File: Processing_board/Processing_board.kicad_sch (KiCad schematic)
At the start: 21 parts, among them J1 Conn_01x06_Pin, J10 Conn_01x03_Pin, J4 Conn_01x02_Pin, J5 Conn_01x08_Pin, J6 Conn_01x08_Pin, J7 Conn_01x02_Pin, J9 Conn_01x03_Pin, SW1 SW_Push, SW2 SW_Push, U1 STM32WBA63CIU6

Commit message: 3 RF antennas
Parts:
- removed D8: IN_S42BT LED, symbol Device:LED
- added D9: IN_S42BT LED, symbol Device:LED
- added R14, R15, R16, R17, R18: 100R, symbol Device:R_Small
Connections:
- net 3.3V: no longer J1.2 (Pin_2), SW2.1
- net GND: now also J1.2 (Pin_2), R18.1; no longer J1.1 (Pin_1)
- net LED: now also D9.2 (A)
- net USART2_RX: now also R15.1; no longer U1.23 (PB4)
- net USART2_TX: now also R14.1; no longer U1.32 (PB0)
- net ANT_LOGIC_2: now reaches U1.10 (PA2)
- net ANT_LOGIC_1: now reaches U1.12 (PA1)
- net RF: now reaches U1.37 (RF)
- net at U1.6 (PA7): now also R17.2; no longer J9.3 (Pin_3)
- net at U1.9 (PA5): now also R16.2; no longer J9.2 (Pin_2)
- new net: R15.2, U1.23 (PB4)
- new net: R14.2, U1.32 (PB0)
- new net: D9.1 (K), R18.2
- new net +3.3V: J1.1 (Pin_1), SW2.1
- new net USART3_RX: J9.3 (Pin_3), R17.1
- new net USART3_TX: J9.2 (Pin_2), R16.1
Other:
- added sheet RF circuitry & antennas (RF.kicad_sch)
- note added: "GND"
- note added: "The 100R resistor is ESD protection apparently"
- note added: "VCC"
- moved on the sheet: J1, J10, J9

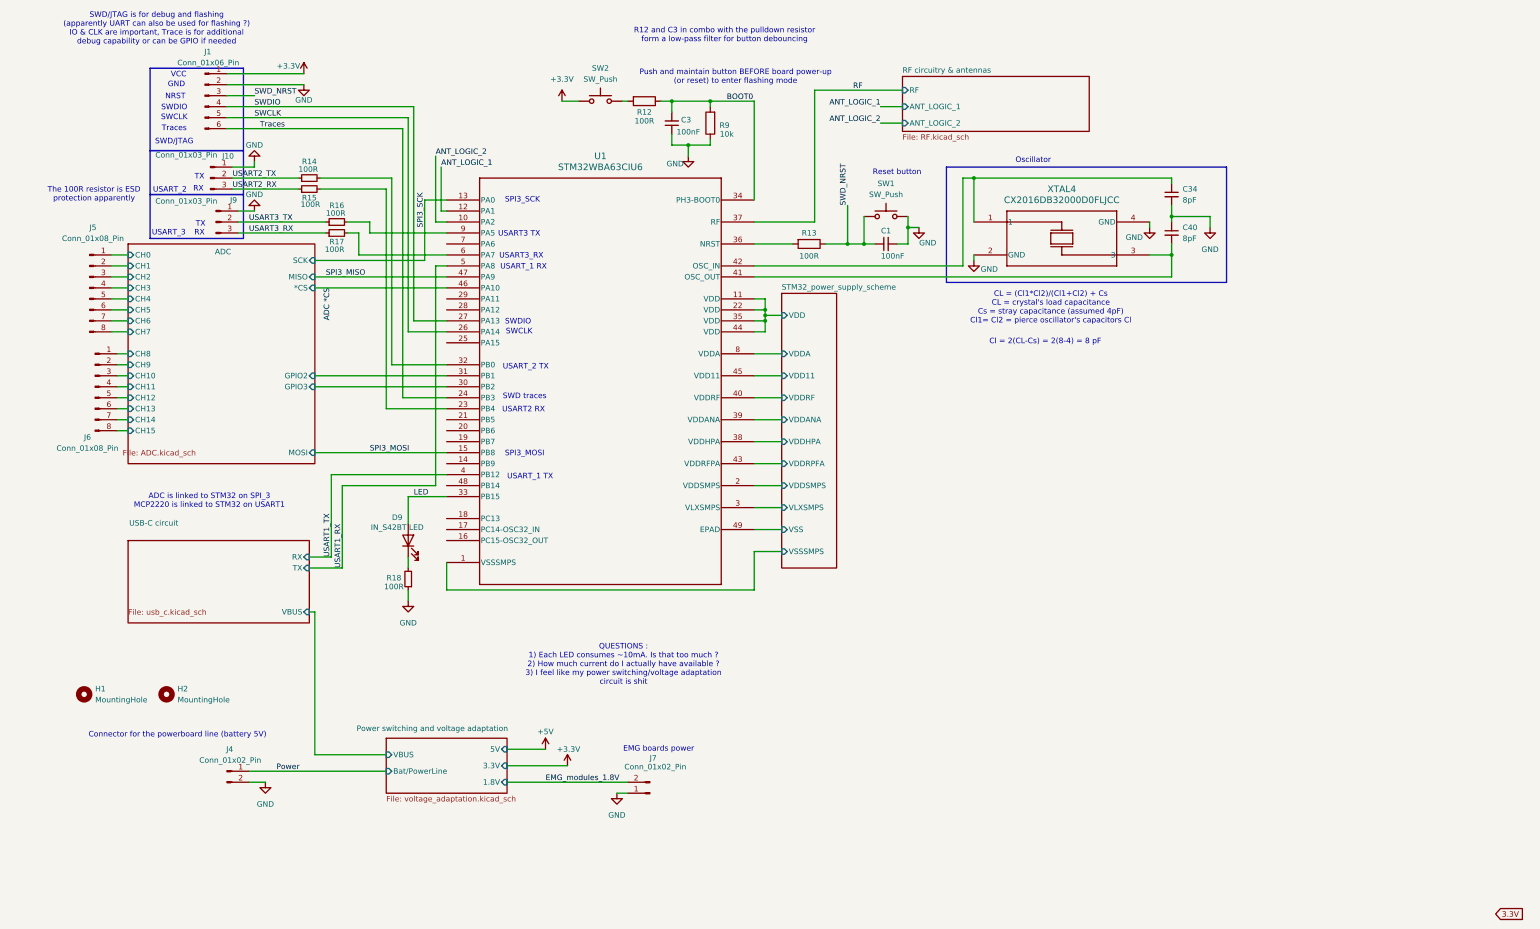
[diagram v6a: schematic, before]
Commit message: added all footprints, ready (?) to design PCB
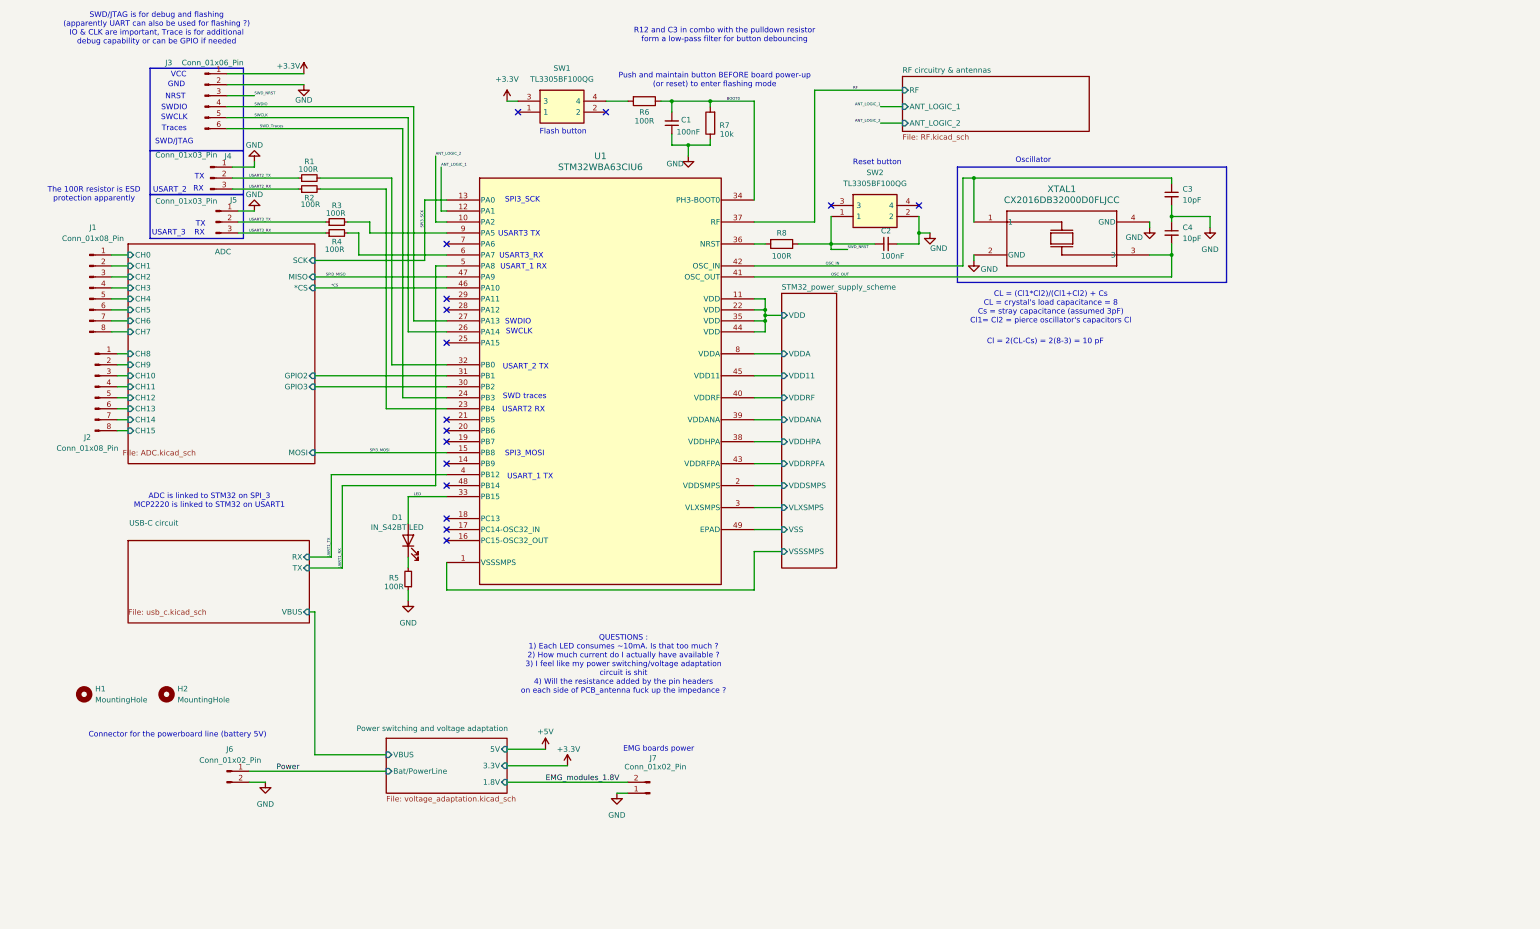
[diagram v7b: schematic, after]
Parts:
- removed SW1, SW2: SW_Push, symbol Switch:SW_Push
- added SW1, SW2: TL3305BF100QG, TL3305BF100QG:TL3305BF160QG, symbol TL3305BF100QG:TL3305BF100QG
- C1: renamed from C3; footprint (none) -> Capacitor_SMD:C_0402_1005Metric
- C2: renamed from C1; footprint (none) -> Capacitor_SMD:C_0402_1005Metric
- C3: renamed from C34; value 8pF -> 10pF; footprint (none) -> Capacitor_SMD:C_0603_1608Metric
- C4: renamed from C40; value 8pF -> 10pF; footprint (none) -> Capacitor_SMD:C_0603_1608Metric
- D1: renamed from D9; footprint (none) -> LED_SMD:LED_0402_1005Metric
- H1, H2: footprint (none) -> MountingHole:MountingHole_2.2mm_M2
- J1: renamed from J5; footprint (none) -> Connector_PinHeader_2.54mm:PinHeader_1x08_P2.54mm_Vertical_SMD_Pin1Left
- J2: renamed from J6; footprint (none) -> Connector_PinHeader_2.54mm:PinHeader_1x08_P2.54mm_Vertical_SMD_Pin1Left
- J3: renamed from J1; footprint (none) -> Connector_PinHeader_2.54mm:PinHeader_1x06_P2.54mm_Vertical_SMD_Pin1Left
- J4: renamed from J10; footprint (none) -> Connector_PinHeader_2.54mm:PinHeader_1x03_P2.54mm_Vertical_SMD_Pin1Left
- J5: renamed from J9; footprint (none) -> Connector_PinHeader_2.54mm:PinHeader_1x03_P2.54mm_Vertical_SMD_Pin1Left
- J6: renamed from J4; footprint (none) -> Connector_PinHeader_2.54mm:PinHeader_1x02_P2.54mm_Vertical_SMD_Pin1Left
- J7: footprint (none) -> Connector_PinHeader_2.54mm:PinHeader_1x02_P2.54mm_Vertical_SMD_Pin1Left
- R1: renamed from R14; footprint (none) -> Resistor_SMD:R_0402_1005Metric
- R2: renamed from R15; footprint (none) -> Resistor_SMD:R_0402_1005Metric
- R3: renamed from R16; footprint (none) -> Resistor_SMD:R_0402_1005Metric
- R4: renamed from R17; footprint (none) -> Resistor_SMD:R_0402_1005Metric
- R5: renamed from R18; footprint (none) -> Resistor_SMD:R_0402_1005Metric
- R6: renamed from R12; footprint (none) -> Resistor_SMD:R_0402_1005Metric
- R7: renamed from R9; footprint (none) -> Resistor_SMD:R_0402_1005Metric
- R8: renamed from R13; footprint (none) -> Resistor_SMD:R_0402_1005Metric
- U1: footprint UFQFPN-48_STM -> SMT32WBA63:UFQFPN-48_STM
- XTAL1: renamed from XTAL4; footprint xtal4_CX2016DB_AVX -> CX2016DB32000D0FLJCC:xtal4_CX2016DB_AVX
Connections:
- net +3.3V: now also SW1.3
- net GND: now also SW2.2
- net SWD_NRST: now also SW2.1
- net at R6.2: now also SW1.4
- net OSC_OUT: now reaches C4.2, U1.41 (OSC_OUT), XTAL1.3
- net OSC_IN: now reaches C3.1, U1.42 (OSC_IN), XTAL1.1
- net ADC *CS renamed *CS
- net Traces renamed SWD_Traces
- net USART1_RX renamed UART1_RX
- net USART1_TX renamed UART1_TX
- no-connect marks 0 -> 16
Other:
- note added: "CL = (Cl1*Cl2)/(Cl1+Cl2) + Cs CL = crystal's load capacitance = 8 Cs = stray capacitance (assumed 3pF) Cl1= Cl2 = pierce oscillator's capacitors Cl"
- note added: "Cl = 2(CL-Cs) = 2(8-3) = 10 pF"
- note added: "Flash button"
- note added: "QUESTIONS : 1) Each LED consumes ~10mA. Is that too much ? 2) How much current do I actually have available ? 3) I feel like my power switching/voltage adaptation circuit is shit 4) Will the resistance added by the pin headers on each side of PCB_antenna fuck up the impedance ?"
- note removed: "CL = (Cl1*Cl2)/(Cl1+Cl2) + Cs CL = crystal's load capacitance Cs = stray capacitance (assumed 4pF) Cl1= Cl2 = pierce oscillator's capacitors Cl"
- note removed: "Cl = 2(CL-Cs) = 2(8-4) = 8 pF"
- note removed: "QUESTIONS : 1) Each LED consumes ~10mA. Is that too much ? 2) How much current do I actually have available ? 3) I feel like my power switching/voltage adaptation circuit is shit"
- moved on the sheet: R8

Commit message: first draft of PCB almost done
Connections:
- net ADC/GPIO2: now also U1.20 (PB6); no longer U1.31 (PB1)
- net ADC/GPIO3: now also U1.19 (PB7); no longer U1.30 (PB2)
- net ANT_LOGIC_1: now also U1.29 (PA11); no longer U1.12 (PA1)
- net ANT_LOGIC_2: now also U1.28 (PA12); no longer U1.10 (PA2)
- net GND: now also J6.1 (Pin_1); no longer J6.2 (Pin_2)
- net Power: now also J6.2 (Pin_2); no longer J6.1 (Pin_1)
- net SPI3_MISO: now also U1.14 (PB9); no longer U1.47 (PA9)
- net USART2_RX: now also R2.2, U1.23 (PB4); no longer J4.3 (Pin_3), R2.1
- net USART2_TX: now also R1.2, U1.32 (PB0); no longer J4.2 (Pin_2), R1.1
- net USART3_RX: now also R4.2, U1.9 (PA5); no longer J5.3 (Pin_3), R4.1
- net USART3_TX: now also R3.2, U1.6 (PA7); no longer J5.2 (Pin_2), R3.1
- net SPI_*CS: now reaches U1.18 (PC13)
- net *CS: no longer names the net of U1.46 (PA10)
- net STM32_power_supply_scheme/VDD11 renamed VDD11
- net STM32_power_supply_scheme/VDDA renamed VDDA
- net STM32_power_supply_scheme/VDDANA renamed VDDANA
- net STM32_power_supply_scheme/VDDHPA renamed VDDHPA
- net STM32_power_supply_scheme/VDDRF renamed VDDRF
- net STM32_power_supply_scheme/VDDRPFA renamed VDDRFPA
- net STM32_power_supply_scheme/VDDSMPS renamed VDDSMPS
- net STM32_power_supply_scheme/VLXSMPS renamed VLXSMPS
- net STM32_power_supply_scheme/VSSSMPS renamed SMPS_VSS
- net UART1_RX renamed USART1_RX
- net UART1_TX renamed USART1_TX
- new net USART2_RX_CONN: J4.3 (Pin_3), R2.1
- new net USART2_TX_CONN: J4.2 (Pin_2), R1.1
- new net USART3_RX_CONN: J5.3 (Pin_3), R4.1
- new net USART3_TX_CONN: J5.2 (Pin_2), R3.1
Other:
- note added: "SPI3_MISO"
- note added: "USART3 RX"
- note added: "USART3_TX"
- note removed: "USART3 TX"
- note removed: "USART3_RX"
- moved on the sheet: R1, R2, R3, R4
